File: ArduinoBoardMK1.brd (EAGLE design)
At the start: 132.1 x 100 mm, 26 parts, among them IC1 TLE5205-2, K1 G5LE, K2 G5LE, K3 G5LE, T1 2N3704, T2 2N3704, T3 2N3704

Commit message: ArduinoBaord MK1 Schematic Complete
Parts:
- removed D1, D3: 1N4004, diode:DO41-10
- removed FAN, PUMP: SMKDSP_1,5/2, con-phoenix-smkdsp:SMKDSP_1,5/2
- removed K1, K3: G5LE, relay:G5LE
- removed R4, R5, R6: (no value), resistor:0207/12
- removed T1, T2, T3: 2N3704, transistor:TO92
- added 12V, DOOR, VIN: SMKDSP_1,5/2, con-phoenix-smkdsp:SMKDSP_1,5/2
- added J1: (no value), SparkFun-Connectors:1X03_LONGPADS
- added OK1: PC817, optocoupler:DIL04
- added X1: 22-23-2021, con-molex:22-23-2021
- R1, R2: value (none) -> 220
- R10, R9: value (none) -> 47k
- R3: value (none) -> 4.7k
- R7, R8: value (none) -> 1k
- moved R10 215.5 mm to (108.0, 62.2), turned to 180 degrees
- moved R9 203.3 mm to (108.0, 49.5)
- moved U$1 203.1 mm to (87.6, 72.4), turned to 180 degrees
- moved PELTIER1 160.1 mm to (144.8, 43.2), turned to 90 degrees
- moved R1 76.7 mm to (99.1, 73.7), turned to 270 degrees
- moved R3 66.0 mm to (83.8, 22.9), turned to 0 degrees
- moved R2 22.4 mm to (117.1, 66.0), turned to 0 degrees
- moved IC1 20.9 mm to (123.2, 55.9)
- moved R7 18.9 mm to (108.0, 53.3)
- moved R8 18.2 mm to (108.0, 58.4)
- moved MOTOR1 8.03 mm to (144.8, 53.3)
- moved U$2 6.35 mm to (113.0, 34.3)
- moved K2 0.35 mm to (118.2, 76.5)
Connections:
- removed net C2: R2.1
- removed net N$11: K3.P, PUMP.1
- removed net N$12: R4.2, R5.2, T3.1
- removed net N$2: D1.A, K1.2, T1.2
- removed net N$23: U$1.A0
- removed net N$24: U$1.A1
- removed net N$8: R2.2, R6.2, T2.1
- removed net N$9: D3.A, K3.2, T3.2
- new net DOORSWITCH: DOOR.2, R3.1, U$1.A2
- new net MOTOR-ENABLE: OK1.1, U$1.D9
- new net MOTOR-ERRORFLAG: IC1.2, U$1.D12
- new net N$21: U$1.D7
- new net N$22: U$1.D8
- new net SCL: U$1.D3, X1.2
- new net SDA: U$1.D2, X1.1
- new net TEMPERATURE: J1.2, U$1.A1
- new net VIN: U$1.VIN, VIN.1
- net +12V: now also 12V.1, R2.2; no longer D1.C, D2.C, D3.C, K1.1, K1.S, K2.1, K3.1, K3.S
- net +5V: now also DOOR.1, J1.3
- net GND: now also 12V.2, J1.1, OK1.3, R1.1, R3.2, U$1.GND, U$1.GND1, VIN.2; no longer FAN.2, PUMP.2, R3.1, R4.1, R6.1, T1.3, T2.3, T3.3
- net MOTOR-IN1: now also U$1.D10
- net MOTOR-IN2: now also U$1.D11
- net N$1: now also OK1.2; no longer R3.2, T1.1
- net N$16: now also PELTIER1.1; no longer PELTIER1.2
- net N$17: now also PELTIER1.2; no longer PELTIER1.1
- net N$3: now also OK1.4; no longer T2.2
- net N$5: now also D2.C, K2.1, R2.1; no longer FAN.1, K1.P
- net PELTIER-CURRENT: now also U$1.A0
- net PELTIER-INA: now also U$1.D6
- net PELTIER-INB: now also U$1.D4
- net PELTIER-PWM: now also U$1.D5
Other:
- board size 132.1 x 100 mm -> 134.6 x 101.3 mm

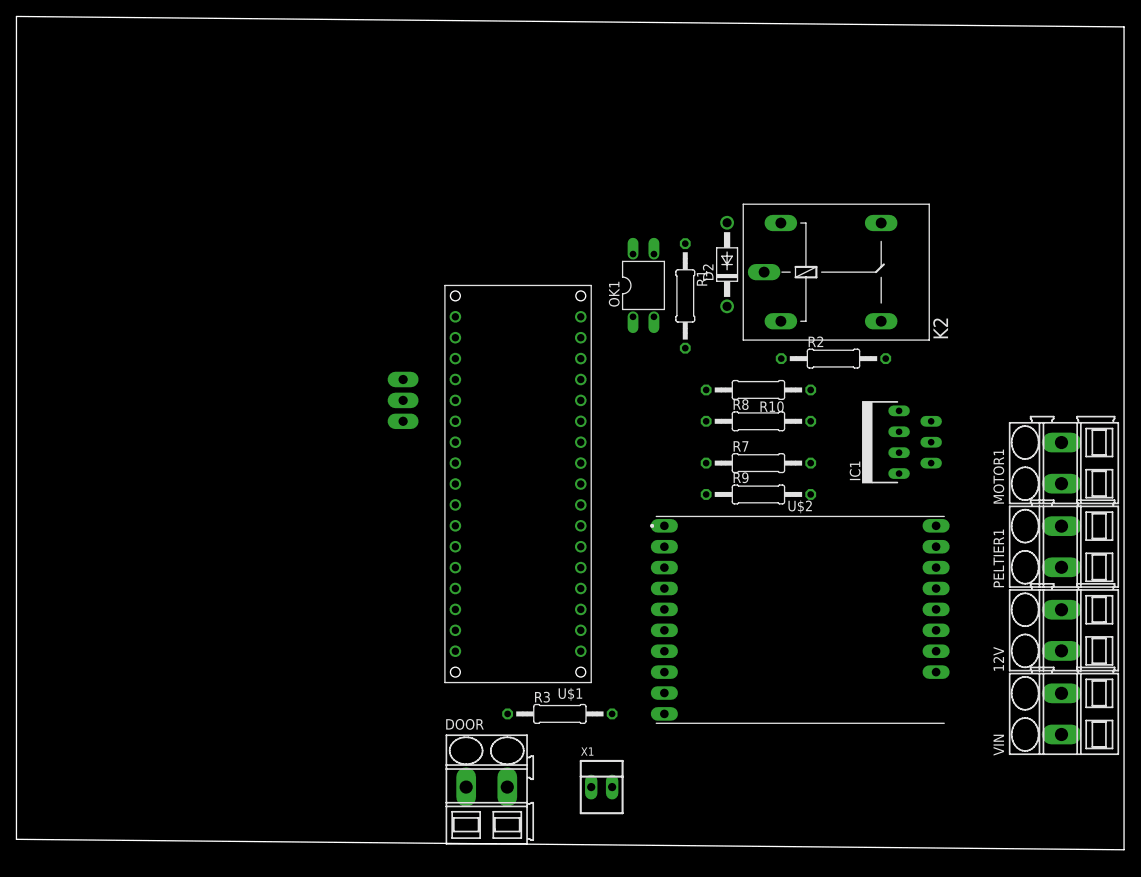
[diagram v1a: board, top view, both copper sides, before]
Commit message: Arduino Board PCB Layout
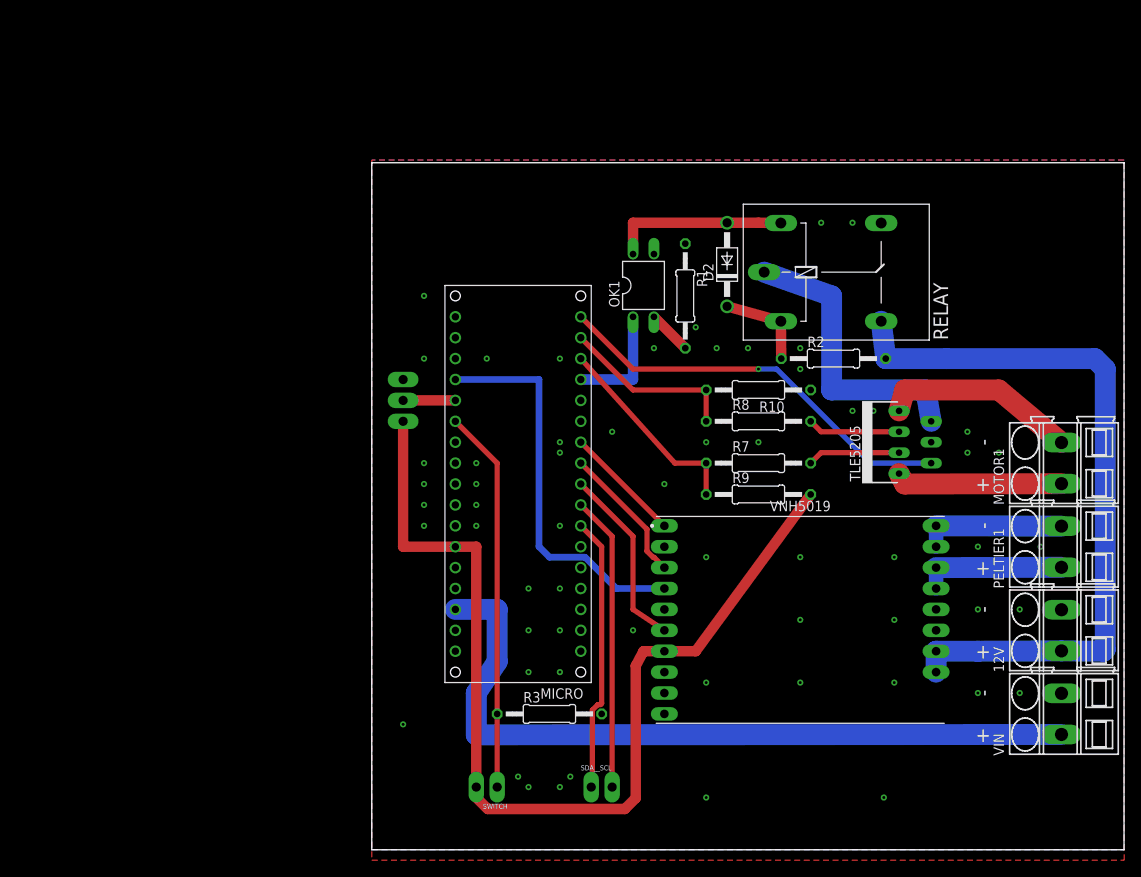
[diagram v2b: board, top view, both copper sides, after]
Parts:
- removed DOOR: SMKDSP_1,5/2, con-phoenix-smkdsp:SMKDSP_1,5/2
- removed X1: 22-23-2021, con-molex:22-23-2021
- added SDA__SCL, SWITCH: (no value), SparkFun-Connectors:1X02_LONGPADS
- moved R3 1.27 mm to (82.5, 22.9)
- renumbered IC1 to TLE5205, K2 to RELAY, U$1 to MICRO, U$2 to VNH5019
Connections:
- net +5V: now also SWITCH.2; no longer DOOR.1
- net DOORSWITCH: now also SWITCH.1; no longer DOOR.2
- net SCL: now also SDA__SCL.2; no longer X1.2
- net SDA: now also SDA__SCL.1; no longer X1.1
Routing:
- net +5V: track 0.00 -> 123.2 mm
- net VIN: track 0.00 -> 92.2 mm
- net +12V: track 0.00 -> 89.0 mm
- net MOTOR-ERRORFLAG: track 0.00 -> 49.9 mm, vias 0 -> 1
- net PELTIER-CURRENT: track 0.00 -> 47.8 mm
- net DOORSWITCH: track 0.00 -> 46.6 mm
- net SCL: track 0.00 -> 35.9 mm
- net N$4: track 0.00 -> 35.4 mm
- net SDA: track 0.00 -> 33.3 mm
- net MOTOR-IN1: track 0.00 -> 24.7 mm
- net N$7: track 0.00 -> 24.0 mm
- net PELTIER-INB: track 0.00 -> 22.4 mm
- net N$3: track 0.00 -> 21.8 mm
- net MOTOR-IN2: track 0.00 -> 21.7 mm
- net N$6: track 0.00 -> 20.5 mm
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- added copper zone on layer 1, net GND
- added copper zone on layer 16, net GND
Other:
- board size 134.6 x 101.3 mm -> 91.4 x 83.5 mm
- board text added: "+"
- board text added: "-"

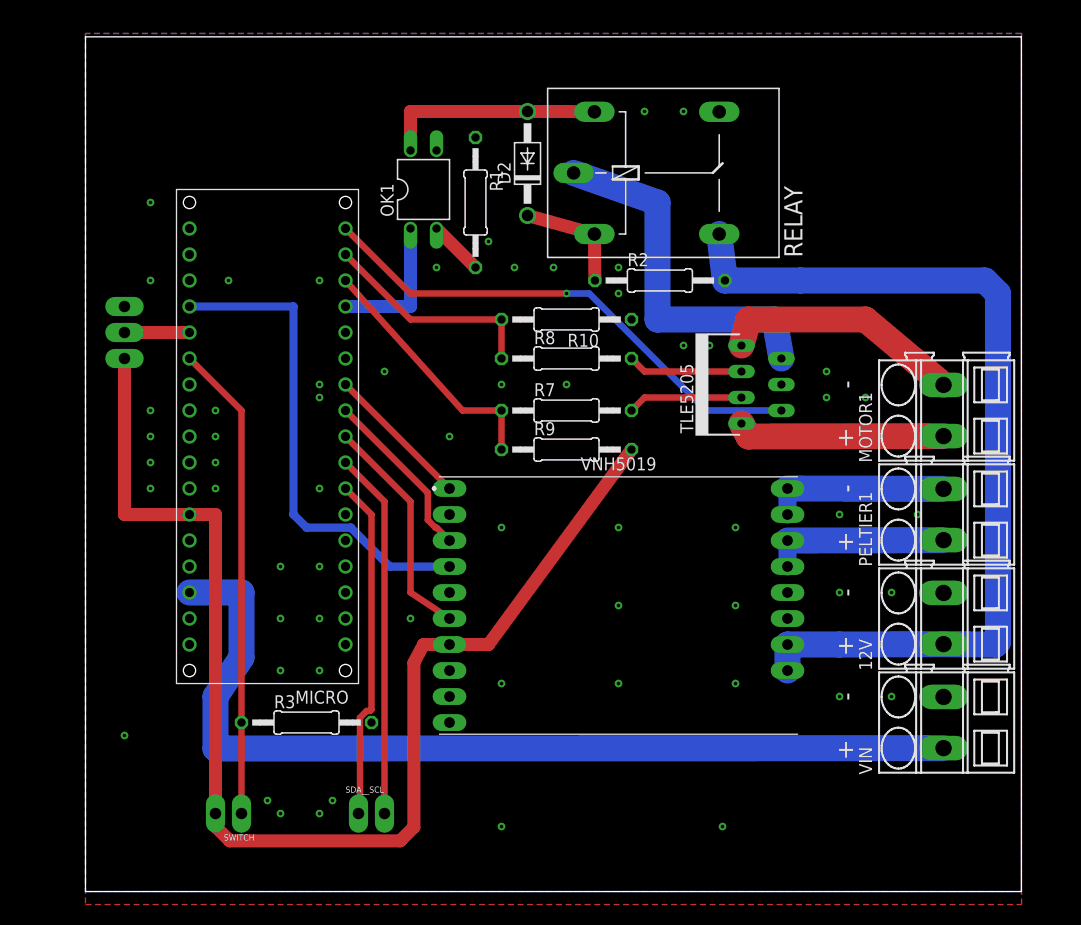
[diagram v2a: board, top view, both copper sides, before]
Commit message: Updated PCB VIAS +more
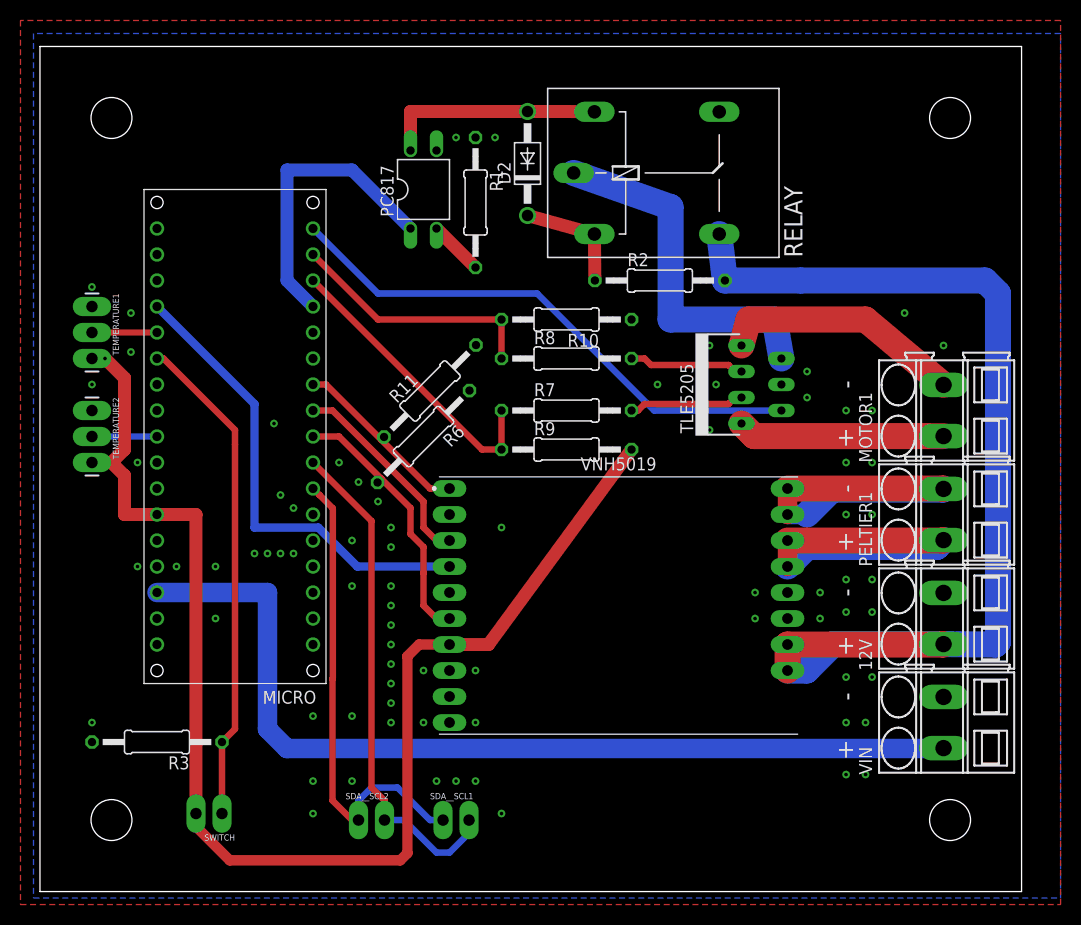
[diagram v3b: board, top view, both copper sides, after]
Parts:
- removed J1: (no value), SparkFun-Connectors:1X03_LONGPADS
- removed SDA__SCL: (no value), SparkFun-Connectors:1X02_LONGPADS
- added R11, R6: 47k, resistor:0207/12
- added SDA__SCL1, SDA__SCL2: (no value), SparkFun-Connectors:1X02_LONGPADS
- added TEMPERATURE1, TEMPERATURE2: (no value), SparkFun-Connectors:1X03_LONGPADS
- moved R3 14.7 mm to (67.9, 21.0), turned to 180 degrees
- moved MICRO 3.17 mm to (84.5, 72.4)
- moved SWITCH 1.91 mm to (74.3, 14.0)
- renumbered OK1 to PC817
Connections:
- removed net N$14: VNH5019.ENA
- removed net N$18: VNH5019.ENB
- removed net TEMPERATURE: J1.2, MICRO.A1
- new net TEMPERATURE1: MICRO.A1, TEMPERATURE1.2
- new net TEMPERATURE2: MICRO.A5, TEMPERATURE2.2
- net +5V: now also TEMPERATURE1.3, TEMPERATURE2.3; no longer J1.3
- net GND: now also R11.2, R6.1, TEMPERATURE1.1, TEMPERATURE2.1; no longer J1.1
- net PELTIER-INA: now also R11.1
- net PELTIER-INB: now also R6.2
- net SCL: now also SDA__SCL1.2, SDA__SCL2.2; no longer SDA__SCL.2
- net SDA: now also SDA__SCL1.1, SDA__SCL2.1; no longer SDA__SCL.1
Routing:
- net N$16: track 17.8 -> 34.1 mm
- net +12V: track 89.0 -> 105.3 mm
- net N$17: track 17.8 -> 34.1 mm
- net MOTOR-ENABLE: track 14.0 -> 28.8 mm
- net SCL: track 35.9 -> 49.4 mm
- net SDA: track 33.3 -> 46.6 mm
- net +5V: track 123.2 -> 131.3 mm, vias 0 -> 1
- net TEMPERATURE: track 6.35 -> 0.00 mm
- net TEMPERATURE2: track 0.00 -> 6.35 mm
- net TEMPERATURE1: track 0.00 -> 6.35 mm
- net MOTOR-IN1: track 24.7 -> 29.1 mm
- net PELTIER-INB: track 22.4 -> 26.7 mm
- net PELTIER-INA: track 14.4 -> 17.9 mm
- net MOTOR-IN2: track 21.7 -> 24.9 mm
- net MOTOR-ERRORFLAG: track 49.9 -> 53.1 mm, vias 1 -> 0
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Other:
- board size 91.4 x 83.5 mm -> 95.9 x 82.6 mm

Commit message: Net Lables + Pull-Down Resistors on Electron
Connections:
- net N$1 renamed POST-OPTO-DIODE
- net N$10 renamed IN1
- net N$13 renamed IN2
- net N$16 renamed PELTIER-OUTB
- net N$17 renamed PELTIER-OUTA
- net N$3 renamed RELAY-TO-OPTO
- net N$4 renamed RELAY-TO-MOTORCONTROLLER
- net N$5 renamed FLYBACK-DIODE+
- net N$6 renamed MOTOR-OUT1
- net N$7 renamed MOTOR-OUT2
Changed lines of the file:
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@@
 <wire x1="133.985" y1="30.52" x2="144.78" y2="30.52" width="2.54" layer="16"/>
 </signal>
-<signal name="N$3">
+<signal name="RELAY-TO-OPTO">
 <contactref element="RELAY" pad="2"/>
 <contactref element="D2" pad="A"/>
@@
 <wire x1="107.95" y1="82.55" x2="104.14" y2="82.55" width="1.27" layer="1"/>
 </signal>
-<signal name="N$4">
+<signal name="RELAY-TO-MOTORCONTROLLER">
 <contactref element="TLE5205" pad="6"/>
 <contactref element="RELAY" pad="P"/>
@@
 <wire x1="128.94" y1="58.42" x2="128.27" y2="62.23" width="2.54" layer="16"/>
 </signal>
-<signal name="N$10">
+<signal name="IN1">
 <contactref element="TLE5205" pad="3"/>
 <contactref element="R7" pad="2"/>
@@
 <wire x1="124.405" y1="54.61" x2="125.04" y2="54.61" width="0.635" layer="1"/>
 </signal>
-<signal name="N$13">
+<signal name="IN2">
 <contactref element="TLE5205" pad="5"/>
 <contactref element="R8" pad="2"/>
@@
 <wire x1="124.405" y1="57.15" x2="125.04" y2="57.15" width="0.635" layer="1"/>
 </signal>
-<signal name="N$6">
+<signal name="MOTOR-OUT1">
 <contactref element="TLE5205" pad="1"/>
 <contactref element="MOTOR1" pad="1"/>
@@
 <wire x1="126.27" y1="50.84" x2="125.04" y2="52.07" width="2.54" layer="1"/>
 </signal>
-<signal name="N$7">
+<signal name="MOTOR-OUT2">
 <contactref element="TLE5205" pad="7"/>
 <contactref element="MOTOR1" pad="2"/>
@@
 <wire x1="80.645" y1="66.04" x2="83.185" y2="63.5" width="1.27" layer="16"/>
 </signal>
-<signal name="N$16">
+<signal name="PELTIER-OUTB">
 <contactref element="VNH5019" pad="OUTB2"/>
 <contactref element="VNH5019" pad="OUTB1"/>
@@
 <wire x1="131.445" y1="40.005" x2="144.105" y2="40.005" width="2.54" layer="16"/>
 </signal>
-<signal name="N$17">
+<signal name="PELTIER-OUTA">
 <contactref element="VNH5019" pad="OUTA2"/>
 <contactref element="VNH5019" pad="OUTA1"/>
@@
 <wire x1="68.58" y1="58.42" x2="67.945" y2="58.42" width="0.635" layer="1"/>
 </signal>
-<signal name="N$1">
+<signal name="POST-OPTO-DIODE">
 <contactref element="R1" pad="2"/>
 <contactref element="PC817" pad="2"/>
 <wire x1="95.25" y1="71.12" x2="99.06" y2="67.31" width="1.27" layer="1"/>
 </signal>
-<signal name="N$5">
+<signal name="FLYBACK-DIODE+">
 <contactref element="RELAY" pad="1"/>
 <contactref element="D2" pad="C"/>

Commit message: Holes
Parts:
- moved 12V 57.5 mm to (87.6, 26.7)
- moved MOTOR1 57.5 mm to (87.6, 47.0)
- moved PELTIER1 57.5 mm to (87.6, 36.8)
- moved VIN 57.5 mm to (87.6, 16.5)
- moved SDA__SCL1 56.9 mm to (39.4, 6.99)
- moved D2 56.9 mm to (47.6, 71.1)
- moved MICRO 56.9 mm to (27.9, 66.0)
- moved PC817 56.9 mm to (37.5, 68.6)
- moved R1 56.9 mm to (42.5, 67.3)
- moved R10 56.9 mm to (51.4, 55.9)
- moved R6 56.9 mm to (37.5, 44.5)
- moved R7 56.9 mm to (51.4, 47.0)
- moved R8 56.9 mm to (51.4, 52.1)
- moved R9 56.9 mm to (51.4, 43.2)
- moved RELAY 56.9 mm to (61.7, 70.2)
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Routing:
- net +12V: track 105.3 -> 101.6 mm
- net MOTOR-ERRORFLAG: track 53.1 -> 56.1 mm
- net PELTIER-OUTB: track 34.1 -> 32.8 mm
- net PELTIER-OUTA: track 34.1 -> 32.8 mm
- net VIN: track 91.0 -> 90.3 mm
- net MOTOR-OUT1: track 20.2 -> 19.6 mm
- net MOTOR-OUT2: track 24.0 -> 23.4 mm
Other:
- board size 95.9 x 82.6 mm -> 95.2 x 82.5 mm

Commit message: DRC Fixes
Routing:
- net PELTIER-INB: track 26.7 -> 26.0 mm
- net PELTIER-INA: track 17.9 -> 18.6 mm
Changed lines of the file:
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@@
 <setting verticaltext="up"/>
 </settings>
-<grid distance="0.025" unitdist="inch" unit="inch" style="lines" multiple="1" display="no" altdistance="5" altunitdist="mil" altunit="mil"/>
+<grid distance="0.025" unitdist="inch" unit="mil" style="lines" multiple="1" display="no" altdistance="5" altunitdist="mil" altunit="mil"/>
 <layers>
 <layer number="1" name="Top" color="4" fill="1" visible="yes" active="yes"/>
@@
 <contactref element="R3" pad="2"/>
 <contactref element="TEMPERATURE1" pad="1"/>
-<polygon width="0.254" layer="16" isolate="0.635">
+<polygon width="0.254" layer="16" isolate="0.381">
 <vertex x="-0.635" y="83.82"/>
 <vertex x="-0.635" y="-0.635"/>
@@
 <vertex x="99.695" y="83.82"/>
 </polygon>
-<polygon width="0.254" layer="1" isolate="0.635">
+<polygon width="0.127" layer="1" isolate="0.381">
 <vertex x="-1.905" y="85.09"/>
 <vertex x="-1.905" y="-1.27"/>
@@
 <vertex x="99.695" y="85.09"/>
 </polygon>
-<via x="65.405" y="45.085" extent="1-16" drill="0.35" shape="octagon"/>
+<via x="65.405" y="45.72" extent="1-16" drill="0.35" shape="octagon"/>
 <via x="8.89" y="52.705" extent="1-16" drill="0.35" shape="octagon"/>
 <via x="45.085" y="35.56" extent="1-16" drill="0.35"/>
@@
 <wire x1="87.63" y1="24.17" x2="92.309" y2="24.133159375" width="2.54" layer="16"/>
 <wire x1="92.309" y1="24.133159375" x2="92.309" y2="57.15" width="2.54" layer="16"/>
-<wire x1="73.025" y1="24.13" x2="87.59" y2="24.13" width="2.54" layer="1"/>
+<wire x1="73.025" y1="24.13" x2="87.59" y2="24.13" width="1.905" layer="1"/>
 <wire x1="87.59" y1="24.13" x2="87.63" y2="24.17" width="2.54" layer="1"/>
-<wire x1="73.025" y1="24.13" x2="73.025" y2="21.59" width="2.54" layer="1"/>
+<wire x1="73.025" y1="24.13" x2="73.025" y2="21.59" width="1.905" layer="1"/>
 <wire x1="73.025" y1="21.59" x2="74.89" y2="21.59" width="2.54" layer="16"/>
 <wire x1="74.89" y1="21.59" x2="77.47" y2="24.17" width="2.54" layer="16"/>
@@
 <contactref element="MICRO" pad="D9"/>
 <contactref element="PC817" pad="1"/>
-<wire x1="24.13" y1="70.485" x2="24.13" y2="59.69" width="1.27" layer="16"/>
+<wire x1="24.13" y1="70.485" x2="24.13" y2="59.055" width="1.27" layer="16"/>
 <wire x1="30.48" y1="70.485" x2="24.13" y2="70.485" width="1.27" layer="16"/>
 <wire x1="36.195" y1="64.77" x2="30.48" y2="70.485" width="1.27" layer="16"/>
-<wire x1="24.13" y1="59.69" x2="26.67" y2="57.15" width="1.27" layer="16"/>
+<wire x1="24.13" y1="59.055" x2="26.035" y2="57.15" width="1.27" layer="16"/>
+<wire x1="26.035" y1="57.15" x2="26.67" y2="57.15" width="1.27" layer="16"/>
 </signal>
 <signal name="PELTIER-OUTB">
@@
 <contactref element="VNH5019" pad="INB"/>
 <wire x1="32.974871875" y1="39.959871875" x2="33.3375" y2="40.3225" width="0.635" layer="1"/>
-<wire x1="39.37" y1="26.67" x2="40.005" y2="26.67" width="0.635" layer="1"/>
 <wire x1="36.195" y1="34.925" x2="37.465" y2="33.655" width="0.635" layer="1"/>
 <wire x1="37.465" y1="33.655" x2="37.465" y2="31.115" width="0.635" layer="1"/>
 <wire x1="37.465" y1="31.115" x2="37.465" y2="27.94" width="0.635" layer="1"/>
 <wire x1="37.465" y1="27.94" x2="38.735" y2="26.67" width="0.635" layer="1"/>
-<wire x1="38.735" y1="26.67" x2="40.005" y2="26.67" width="0.635" layer="1"/>
+<wire x1="38.735" y1="26.67" x2="39.37" y2="26.67" width="0.635" layer="1"/>
+<wire x1="39.37" y1="26.67" x2="40.005" y2="26.67" width="0.635" layer="1"/>
 </signal>
 <signal name="PELTIER-INA">
@@
 <wire x1="38.1" y1="39.37" x2="33.3375" y2="44.1325" width="0.635" layer="1"/>
 <wire x1="33.3375" y1="44.1325" x2="27.94" y2="49.53" width="0.635" layer="1"/>
-<wire x1="33.609871875" y1="44.404875" x2="33.609871875" y2="44.404871875" width="0.635" layer="1"/>
+<wire x1="33.60986875" y1="44.404875" x2="32.974871875" y2="44.404875" width="0.635" layer="1"/>
 <wire x1="33.609871875" y1="44.404871875" x2="33.3375" y2="44.1325" width="0.635" layer="1"/>
+<wire x1="33.60986875" y1="44.404875" x2="33.609871875" y2="44.404871875" width="0.635" layer="1"/>
 </signal>
 <signal name="PELTIER-CURRENT">
